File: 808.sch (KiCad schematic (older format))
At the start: 52 parts

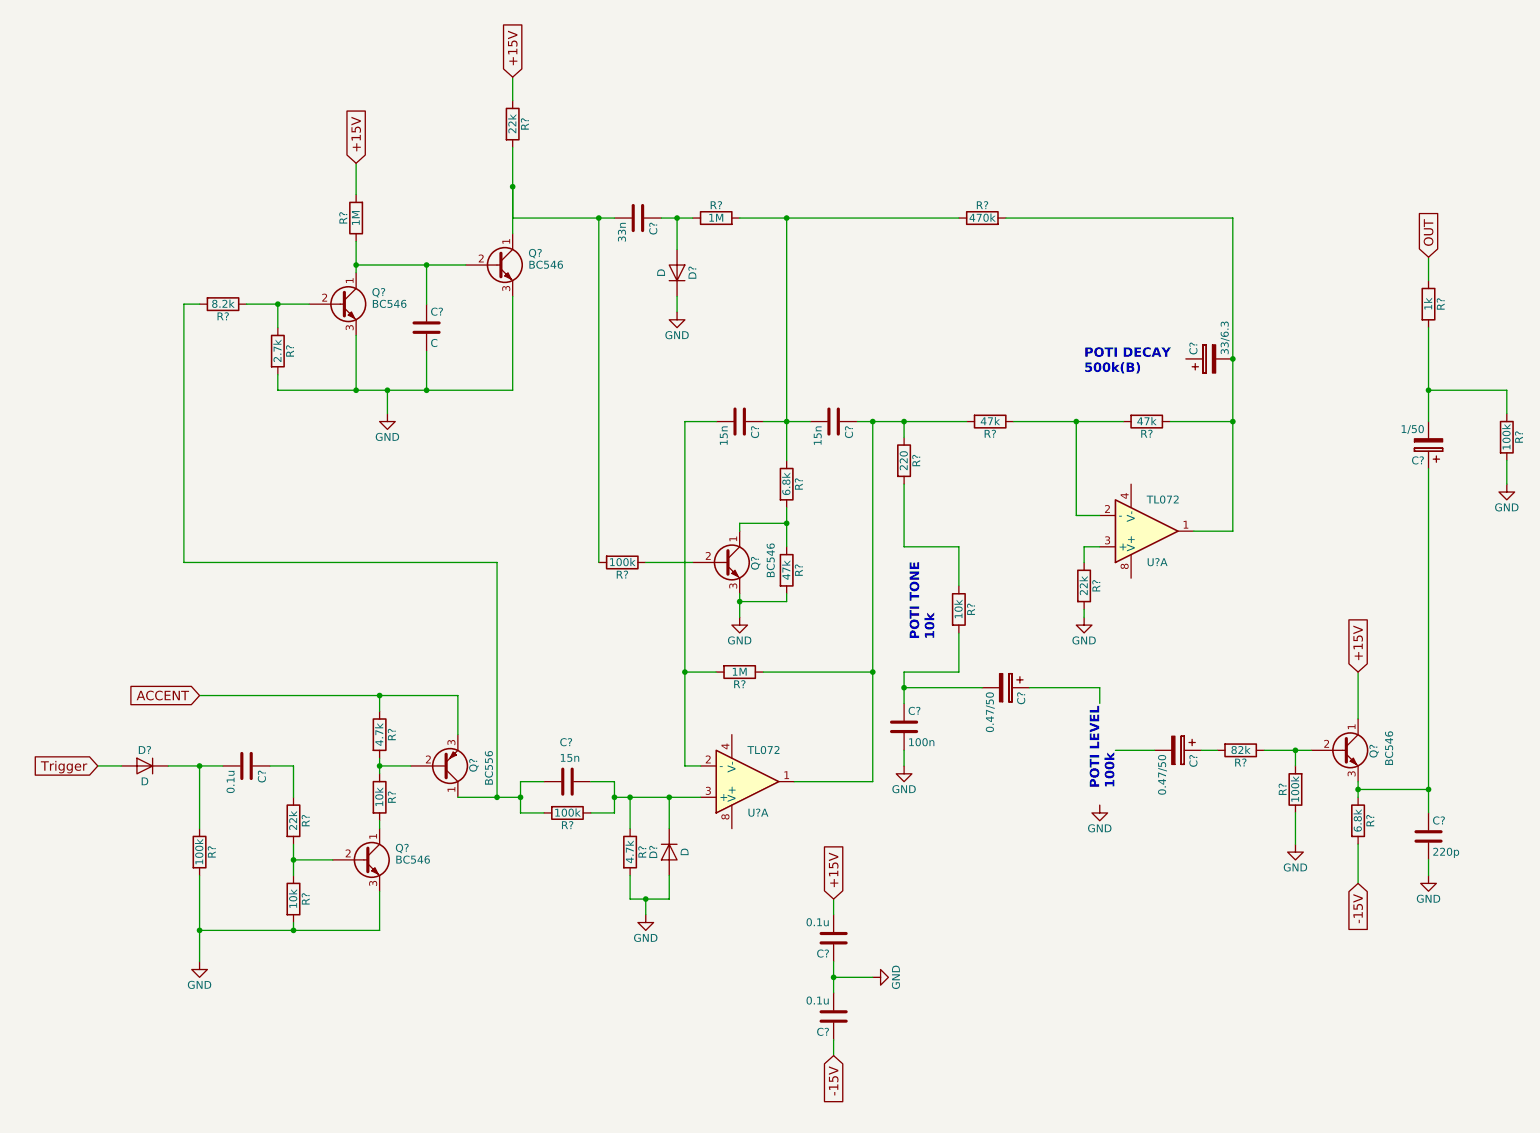
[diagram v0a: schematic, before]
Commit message: Added one of the potis, and some power symbols.
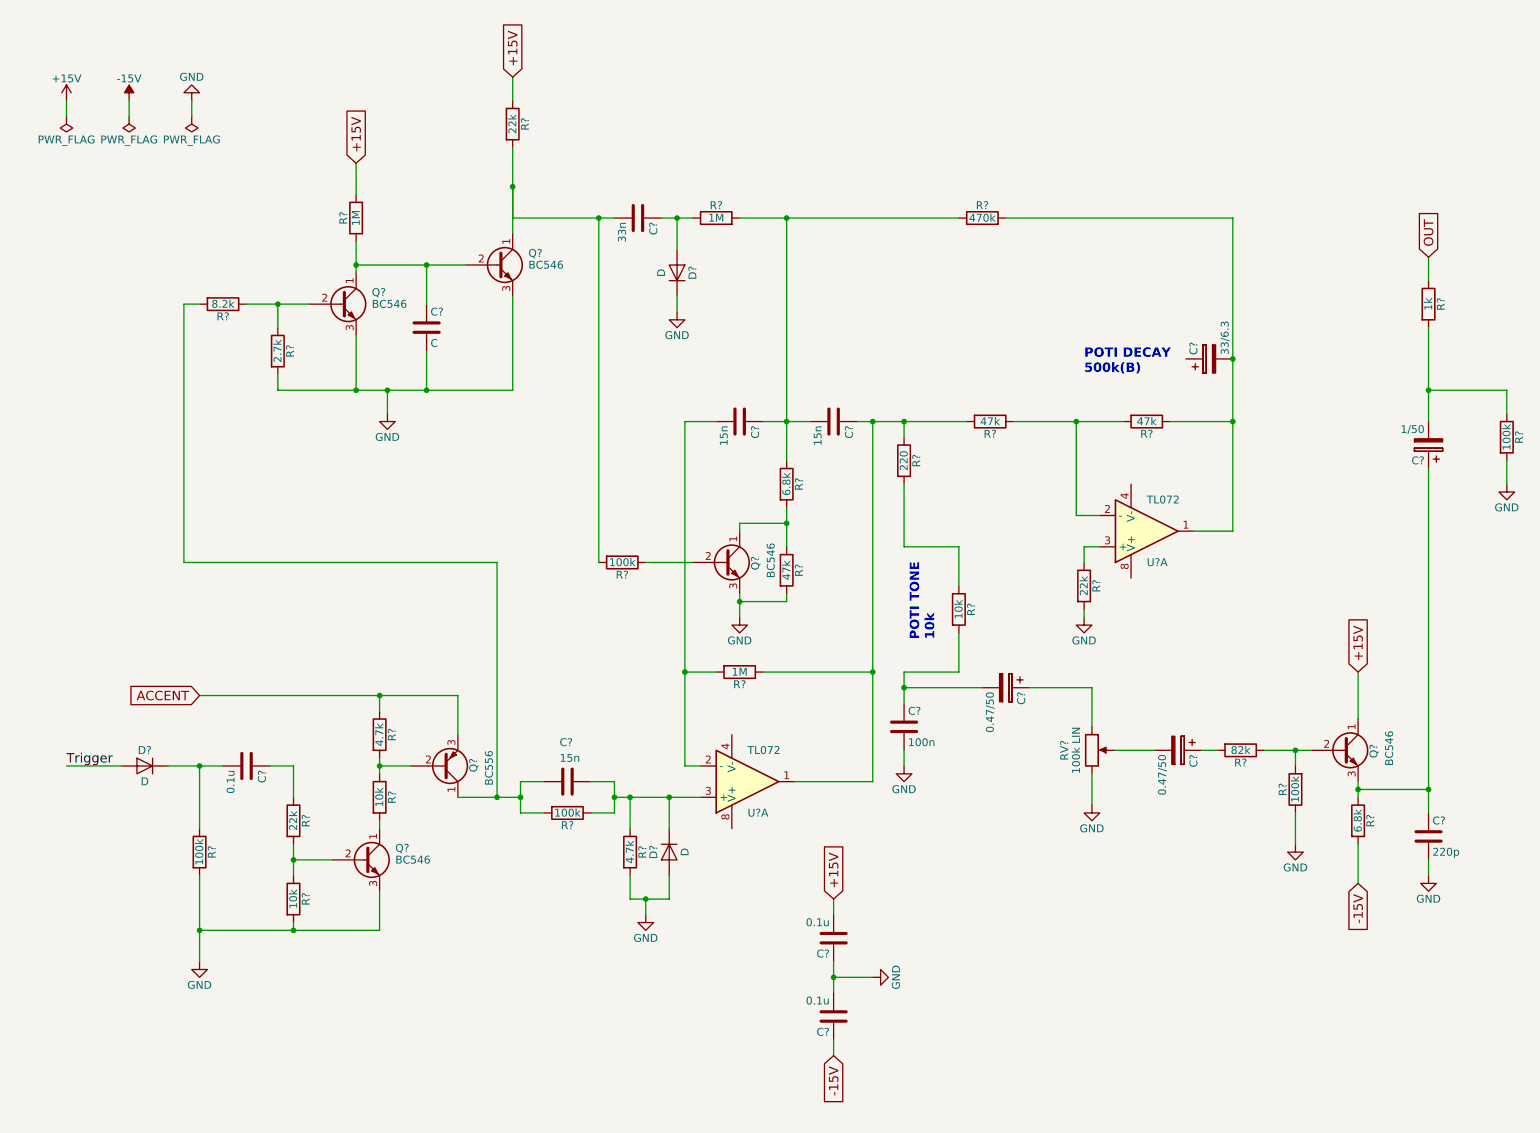
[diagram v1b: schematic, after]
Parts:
- added RV?: 100k LIN, symbol POT
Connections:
- net GND: now also RV?.3
- net at C?.1: now also RV?.1
- net at C?.2: now also RV?.2
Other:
- note removed: "POTI LEVEL\n100k"
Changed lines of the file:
@@
 	-1   0    0    -1
 $EndComp
-Text GLabel 1200 5400 0    60   Input ~ 0
-Trigger
 $Comp
 L GND #PWR?
@@
 	0    1    1    0
 $EndComp
-Text Notes 7700 5550 1    60   ~ 12
-POTI LEVEL\n100k
 $Comp
 L R R?
@@
 L GND #PWR?
 U 1 1 5AB6EF83
-P 7600 5650
-F 0 "#PWR?" H 7600 5400 50  0001 C CNN
-F 1 "GND" H 7600 5500 50  0000 C CNN
-F 2 "" H 7600 5650 50  0001 C CNN
-F 3 "" H 7600 5650 50  0001 C CNN
-	1    7600 5650
+P 7550 5650
+F 0 "#PWR?" H 7550 5400 50  0001 C CNN
+F 1 "GND" H 7550 5500 50  0000 C CNN
+F 2 "" H 7550 5650 50  0001 C CNN
+F 3 "" H 7550 5650 50  0001 C CNN
+	1    7550 5650
 	1    0    0    -1
 $EndComp
@@
 $EndComp
 Wire Wire Line
-	1200 5400 1350 5400
+	1000 5400 1350 5400
 Wire Wire Line
 	1650 5400 2000 5400
@@
 Connection ~ 7450 3200
 Wire Wire Line
-	8200 3900 8450 3900
-Wire Wire Line
-	8450 3900 8450 1900
+	8450 3900 8200 3900
+Wire Wire Line
+	8450 1900 8450 3900
 Wire Wire Line
 	8050 3200 8450 3200
@@
 	5900 7150 5900 7250
 Wire Wire Line
-	7150 4900 7600 4900
-Wire Wire Line
-	7600 4900 7600 5000
+	7150 4900 7550 4900
+Wire Wire Line
+	7550 4900 7550 5150
 Wire Wire Line
 	7950 5300 7700 5300
+$Comp
+L POT RV?
+U 1 1 5AB7F251
+P 7550 5300
+F 0 "RV?" V 7375 5300 50  0000 C CNN
+F 1 "100k LIN" V 7450 5300 50  0000 C CNN
+F 2 "" H 7550 5300 50  0001 C CNN
+F 3 "" H 7550 5300 50  0001 C CNN
+	1    7550 5300
+	1    0    0    -1
+$EndComp
+Wire Wire Line
+	7550 5650 7550 5450
+$Comp
+L +15V #PWR?
+U 1 1 5AB7FD37
+P 1000 1150
+F 0 "#PWR?" H 1000 1000 50  0001 C CNN
+F 1 "+15V" H 1000 1290 50  0000 C CNN
+F 2 "" H 1000 1150 50  0001 C CNN
+F 3 "" H 1000 1150 50  0001 C CNN
+	1    1000 1150
+	1    0    0    -1
+$EndComp
+$Comp
+L -15V #PWR?
+U 1 1 5AB80014
+P 1400 1150
+F 0 "#PWR?" H 1400 1000 50  0001 C CNN
+F 1 "-15V" H 1400 1290 50  0000 C CNN
+F 2 "" H 1400 1150 50  0001 C CNN
+F 3 "" H 1400 1150 50  0001 C CNN
+	1    1400 1150
+	1    0    0    -1
+$EndComp
+$Comp
+L GND #PWR?
+U 1 1 5AB80467
+P 1800 1150
+F 0 "#PWR?" H 1800 900 50  0001 C CNN
+F 1 "GND" H 1800 1000 50  0000 C CNN
+F 2 "" H 1800 1150 50  0001 C CNN
+F 3 "" H 1800 1150 50  0001 C CNN
+	1    1800 1150
+	-1   0    0    1
+$EndComp
+$Comp
+L PWR_FLAG #FLG?
+U 1 1 5AB804E5
+P 1000 1250
+F 0 "#FLG?" H 1000 1325 50  0001 C CNN
+F 1 "PWR_FLAG" H 1000 1400 50  0000 C CNN
+F 2 "" H 1000 1250 50  0001 C CNN
+F 3 "" H 1000 1250 50  0001 C CNN
+	1    1000 1250
+	-1   0    0    1
+$EndComp
+$Comp
+L PWR_FLAG #FLG?
+U 1 1 5AB80596
+P 1400 1250
+F 0 "#FLG?" H 1400 1325 50  0001 C CNN
+F 1 "PWR_FLAG" H 1400 1400 50  0000 C CNN
+F 2 "" H 1400 1250 50  0001 C CNN
+F 3 "" H 1400 1250 50  0001 C CNN
+	1    1400 1250
+	-1   0    0    1
+$EndComp
+$Comp
+L PWR_FLAG #FLG?
+U 1 1 5AB80640
+P 1800 1250
+F 0 "#FLG?" H 1800 1325 50  0001 C CNN
+F 1 "PWR_FLAG" H 1800 1400 50  0000 C CNN
+F 2 "" H 1800 1250 50  0001 C CNN
+F 3 "" H 1800 1250 50  0001 C CNN
+	1    1800 1250
+	-1   0    0    1
+$EndComp
+Wire Wire Line
+	1000 1150 1000 1250
+Wire Wire Line
+	1400 1150 1400 1250
+Wire Wire Line
+	1800 1150 1800 1250
+Text Label 1000 5400 0    60   ~ 0
+Trigger
 $EndSCHEMATC
